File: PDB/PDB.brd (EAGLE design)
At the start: 160 x 101.6 mm, 58 parts, among them Q1 IRFML8244, Q2 IRFML8244, Q3 PMOSFET, Q4 P-CHANNEL-MOSFETSOT23-3, Q5 P-CHANNEL-MOSFETSOT23-3

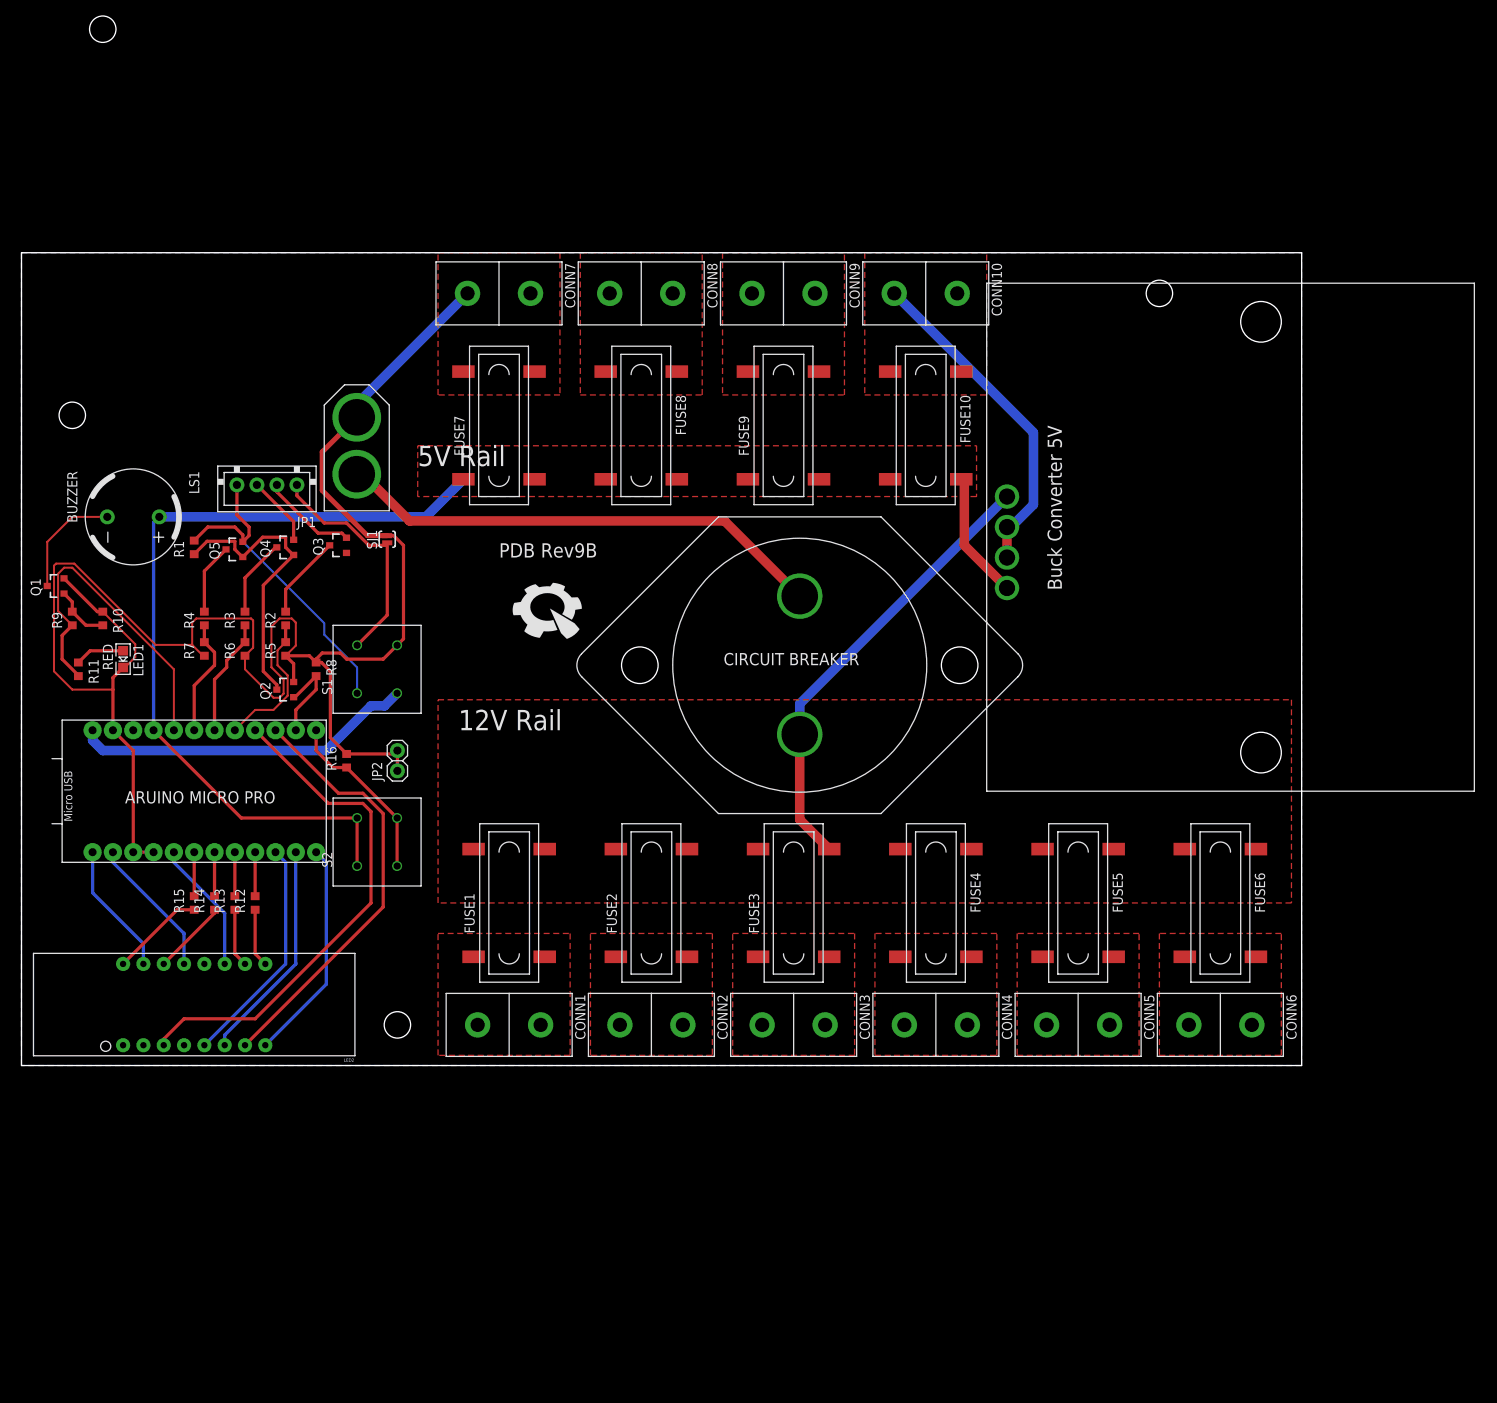
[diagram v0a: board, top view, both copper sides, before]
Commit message: Delete mounting hole; Reroute for XT60 conenction, and fix files
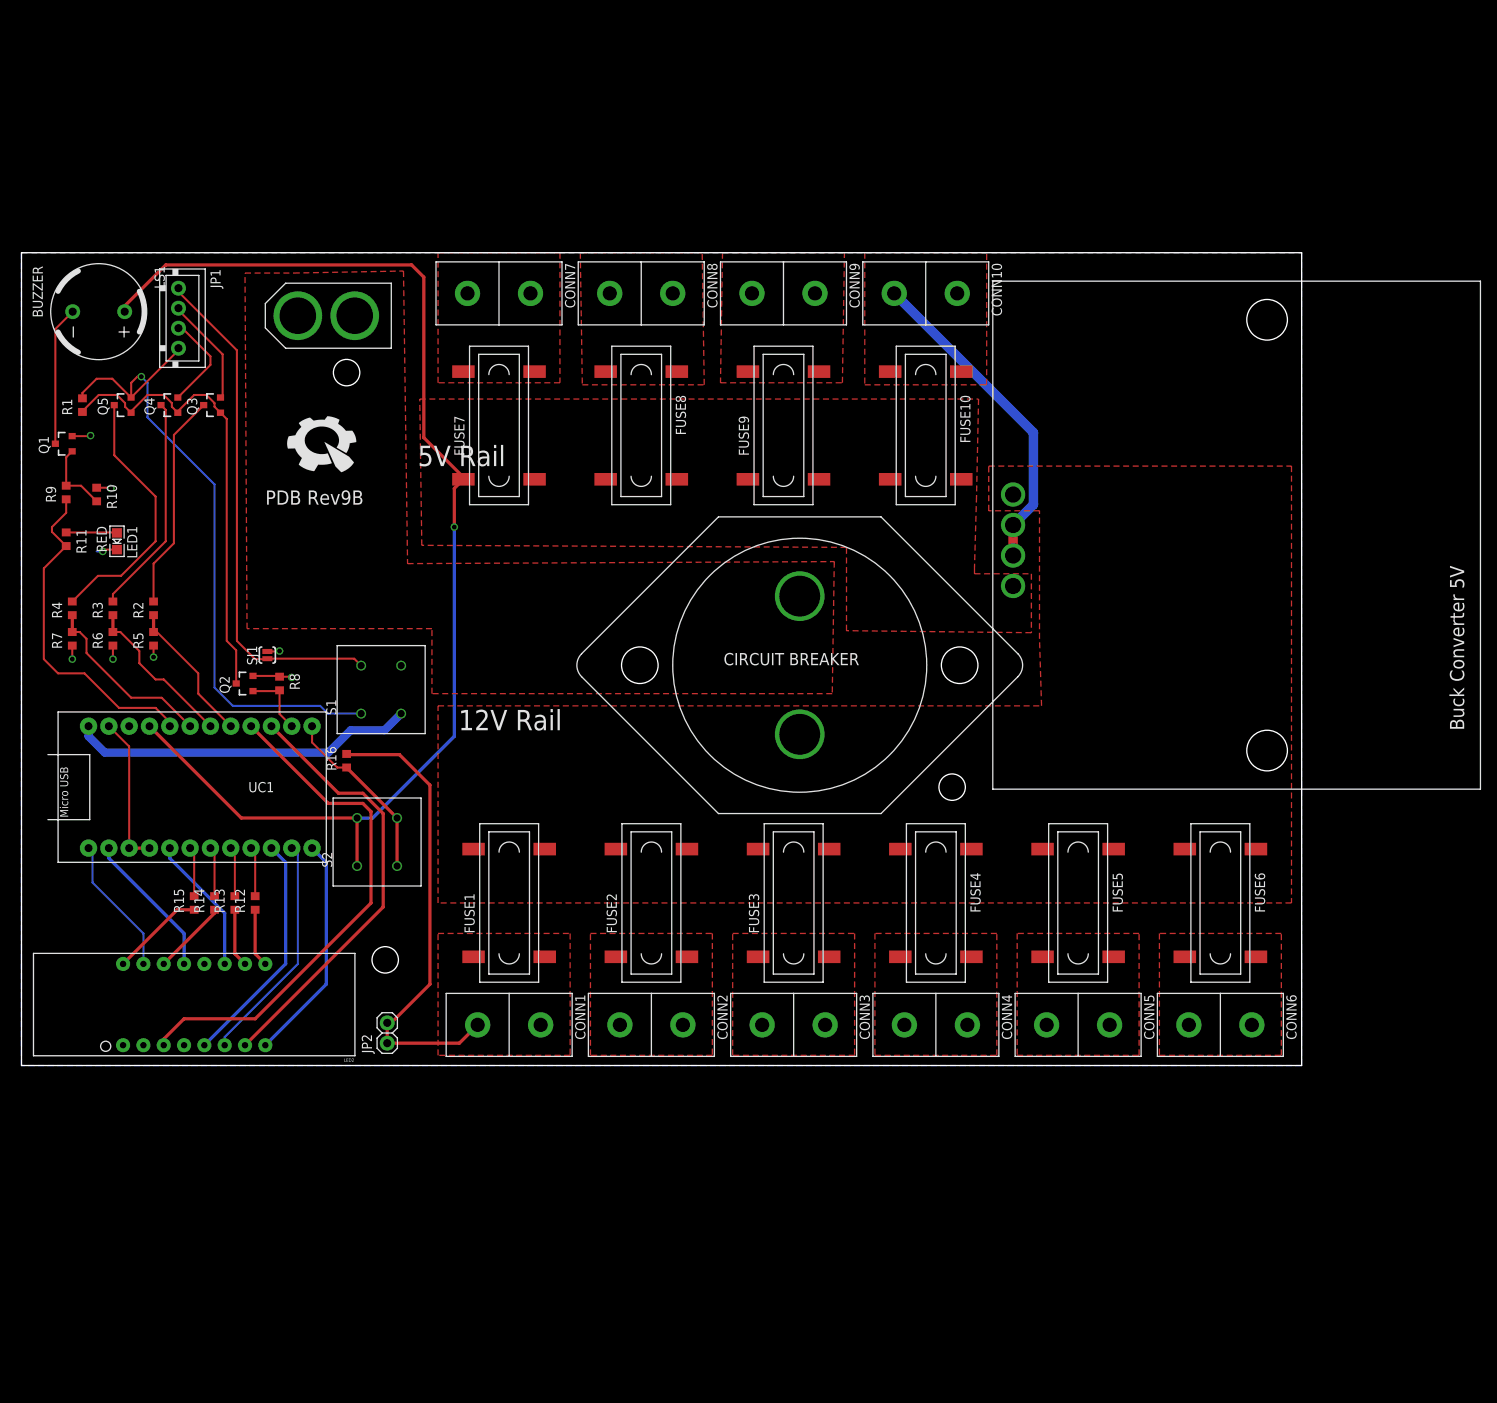
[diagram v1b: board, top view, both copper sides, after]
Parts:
- removed U$3: (no value), pie:STAND-OFF
- moved U$4 66.9 mm to (116.3, 34.8)
- moved U$6 35.1 mm to (37.8, 78.0)
- moved U$5 34.7 mm to (40.6, 86.6)
- moved JP2 34.1 mm to (45.7, 4.06)
- moved LS1 26.0 mm to (9.65, 94.2)
- moved Q3 23.6 mm to (23.9, 82.5)
- moved JP1 23.4 mm to (19.8, 93.2), turned to 270 degrees
- moved Q4 22.9 mm to (18.5, 82.5)
- moved Q5 22.8 mm to (12.7, 82.5)
- moved R1 22.6 mm to (7.62, 82.5)
- moved SJ1 20.8 mm to (30.7, 51.3)
- moved Q1 17.8 mm to (5.33, 77.7)
- moved XT60 16.7 mm to (38.1, 93.7), turned to 180 degrees
- moved R2 16.6 mm to (16.5, 57.1)
- moved R3 16.6 mm to (11.4, 57.1)
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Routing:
- net GND: track 271.6 -> 137.3 mm, vias 0 -> 8
- net BAT: track 61.7 -> 0.00 mm
- net 12V: track 56.3 -> 0.00 mm
- net BCELL3: track 41.0 -> 82.8 mm, vias 0 -> 1
- net 5V: track 118.9 -> 155.3 mm, vias 0 -> 1
- net BGND: track 29.7 -> 64.0 mm
- net N$4: track 8.91 -> 32.7 mm
- net N$1: track 36.3 -> 58.5 mm
- net N$3: track 9.79 -> 27.5 mm
- net N$2: track 10.6 -> 27.1 mm
- net IO2: track 14.7 -> 22.8 mm
- net IO1: track 14.7 -> 20.1 mm
- net BCELL2: track 8.76 -> 12.3 mm
- net DIV_EN: track 11.7 -> 8.47 mm
- net N$5: track 14.3 -> 17.4 mm
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- added copper zone on layer 1, net BAT

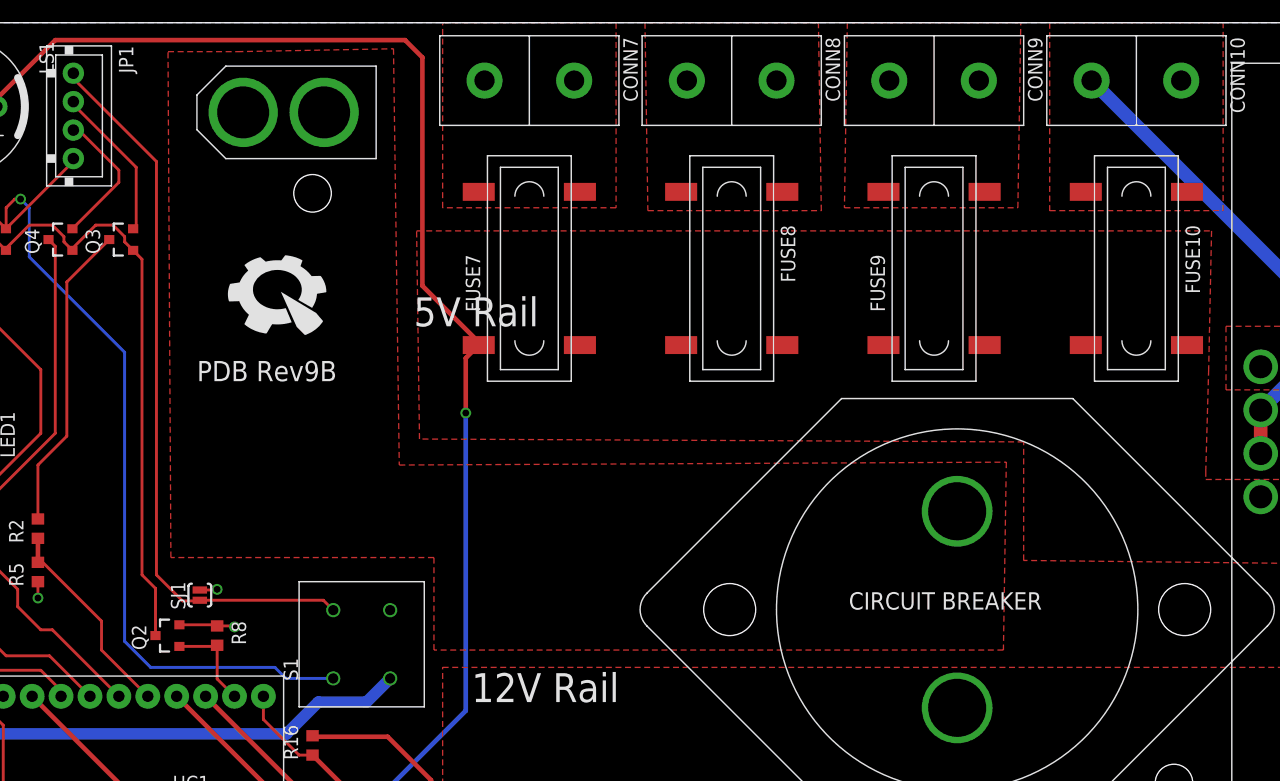
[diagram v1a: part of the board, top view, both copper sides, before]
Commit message: Change width of 5V rail; move U mounting hole
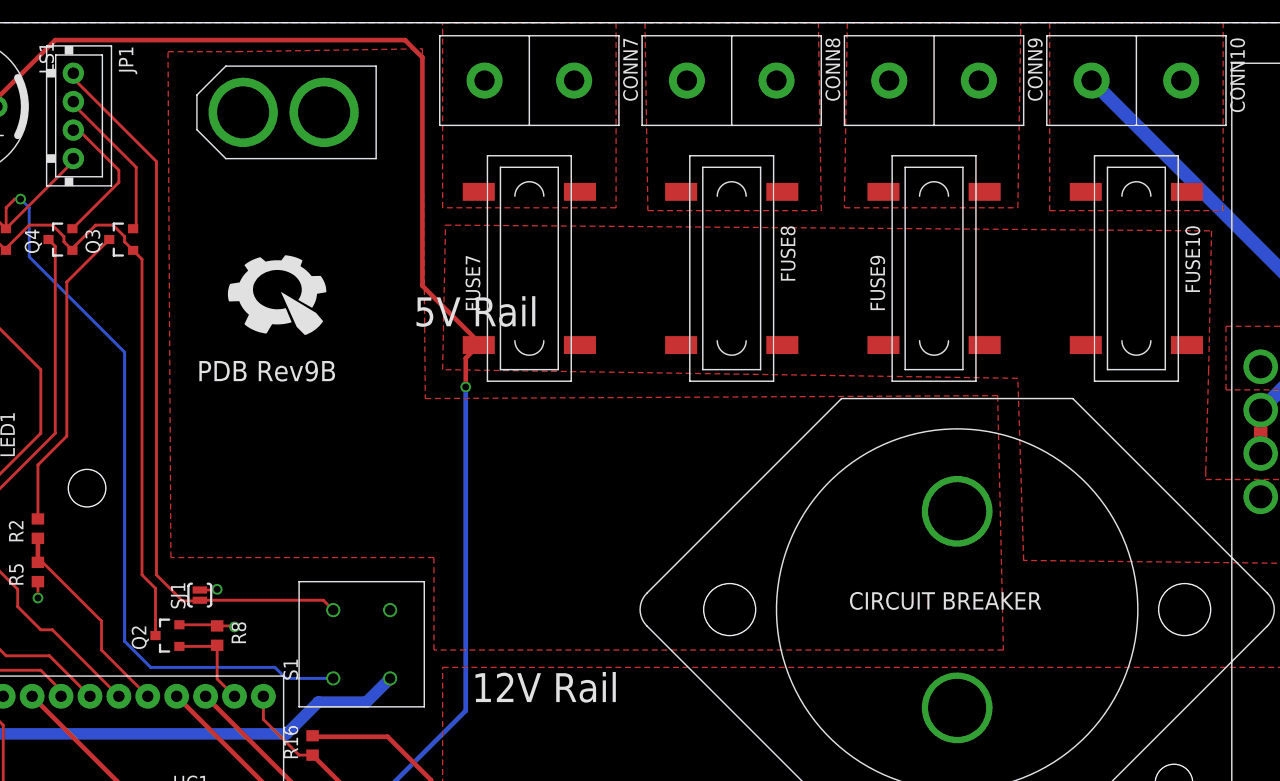
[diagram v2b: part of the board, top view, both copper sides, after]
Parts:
- moved U$5 32.6 mm to (20.8, 60.7)
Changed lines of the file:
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@@
 <element name="U$2" library="pie" package="STAND-OFF" value="" x="45.466" y="13.208"/>
 <element name="U$4" library="pie" package="STAND-OFF" value="" x="116.332" y="34.798" rot="R90"/>
-<element name="U$5" library="pie" package="STAND-OFF" value="" x="40.64" y="86.614"/>
+<element name="U$5" library="pie" package="STAND-OFF" value="" x="20.828" y="60.706"/>
 <element name="U$6" library="pie" package="PIE-LOGO-SMALL" value="" x="37.846" y="77.978"/>
 <element name="U$7" library="pie" package="BUCK_CONVERTER_5V" value="BUCK_CONVERTER_5V" x="155.702" y="66.294" rot="R90"/>
@@
 <contactref element="XT60" pad="12V"/>
 <polygon width="1.1938" layer="1">
-<vertex x="47.752" y="99.314"/>
-<vertex x="48.26" y="62.738"/>
-<vertex x="101.6" y="62.992"/>
+<vertex x="50.292" y="99.314"/>
+<vertex x="50.546" y="68.58"/>
+<vertex x="100.838" y="68.834"/>
 <vertex x="101.346" y="46.482"/>
 <vertex x="51.308" y="46.482"/>
@@
 <contactref element="FUSE7" pad="P$1_DOWN"/>
 <polygon width="1.1938" layer="1">
-<vertex x="49.784" y="83.312"/>
+<vertex x="52.324" y="83.82"/>
 <vertex x="119.634" y="83.312"/>
 <vertex x="119.38" y="71.12"/>
@@
 <vertex x="126.238" y="54.102"/>
 <vertex x="103.124" y="54.356"/>
-<vertex x="103.124" y="64.77"/>
-<vertex x="50.038" y="65.024"/>
+<vertex x="102.616" y="70.358"/>
+<vertex x="52.07" y="71.12"/>
 </polygon>
 <contactref element="LS1" pad="A"/>
@@
 <wire x1="41.95" y1="30.94" x2="43.894" y2="30.94" width="0.4064" layer="16"/>
 <wire x1="43.894" y1="30.94" x2="54.102" y2="41.148" width="0.4064" layer="16"/>
-<wire x1="54.102" y1="41.148" x2="54.102" y2="67.31" width="0.4064" layer="16"/>
-<via x="54.102" y="67.31" extent="1-16" drill="0.6" shape="square"/>
-<wire x1="54.102" y1="67.31" x2="54.102" y2="72.136" width="0.4064" layer="1"/>
+<wire x1="54.102" y1="41.148" x2="54.102" y2="69.596" width="0.4064" layer="16"/>
+<via x="54.102" y="69.596" extent="1-16" drill="0.6" shape="square"/>
+<wire x1="54.102" y1="69.596" x2="54.102" y2="72.136" width="0.4064" layer="1"/>
 <wire x1="54.102" y1="72.136" x2="55.245" y2="73.279" width="0.4064" layer="1"/>
 </signal>

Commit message: Update library parts and fix the text
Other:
- board text added: "Copyright (c) 2016, Pioneers in Engineering All rights reserved. Design by: Sharabesh R, Mohammed H, Tobin H. This design is open source hardware. For more information, visit github.com/pioneers/SmartSensors"
- board text removed: "Copyright (c) 2013, Pioneers in Engineering All rights reserved. Design by: Sharabesh R, Mohammed H, Tobin H. This design is open source hardware. For more information, visit pioneers.berkeley.edu/opensource"
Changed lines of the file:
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@@
 <?xml version="1.0" encoding="utf-8"?>
 <!DOCTYPE eagle SYSTEM "eagle.dtd">
-<eagle version="7.6.0">
+<eagle version="7.7.0">
 <drawing>
 <settings>
@@
 <wire x1="160.02" y1="101.6" x2="0" y2="101.6" width="0" layer="20"/>
 <wire x1="0" y1="101.6" x2="0" y2="0" width="0" layer="20"/>
-<text x="92.202" y="39.116" size="1.524" layer="22" font="vector" rot="MR0">Copyright (c) 2013, Pioneers in Engineering
+<text x="92.71" y="52.832" size="1.524" layer="22" font="vector" rot="MR0">Copyright (c) 2016, Pioneers in Engineering
 All rights reserved.
 Design by: Sharabesh R, Mohammed H, Tobin H.
 This design is open source hardware.
 For more information, visit
-pioneers.berkeley.edu/opensource</text>
+github.com/pioneers/SmartSensors</text>
 <text x="30.48" y="70.104" size="1.778" layer="21" font="vector">PDB Rev9B</text>
 <text x="54.61" y="41.91" size="2.54" layer="21" font="vector">12V Rail</text>
